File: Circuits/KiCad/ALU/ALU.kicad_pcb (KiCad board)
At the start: 2 copper layers, 131.4 x 86.4 mm, 30 parts, among them J1 Conn_01x13_Male, J2 Conn_01x13_Male, U1 74x377, U10 74x08, U11 74x27, U12 74x245, U2 74x377, U3 74x04, U4 74x181, U5 74x181, U6 74x245, U7 74x08, U8 74x32, U9 74x27

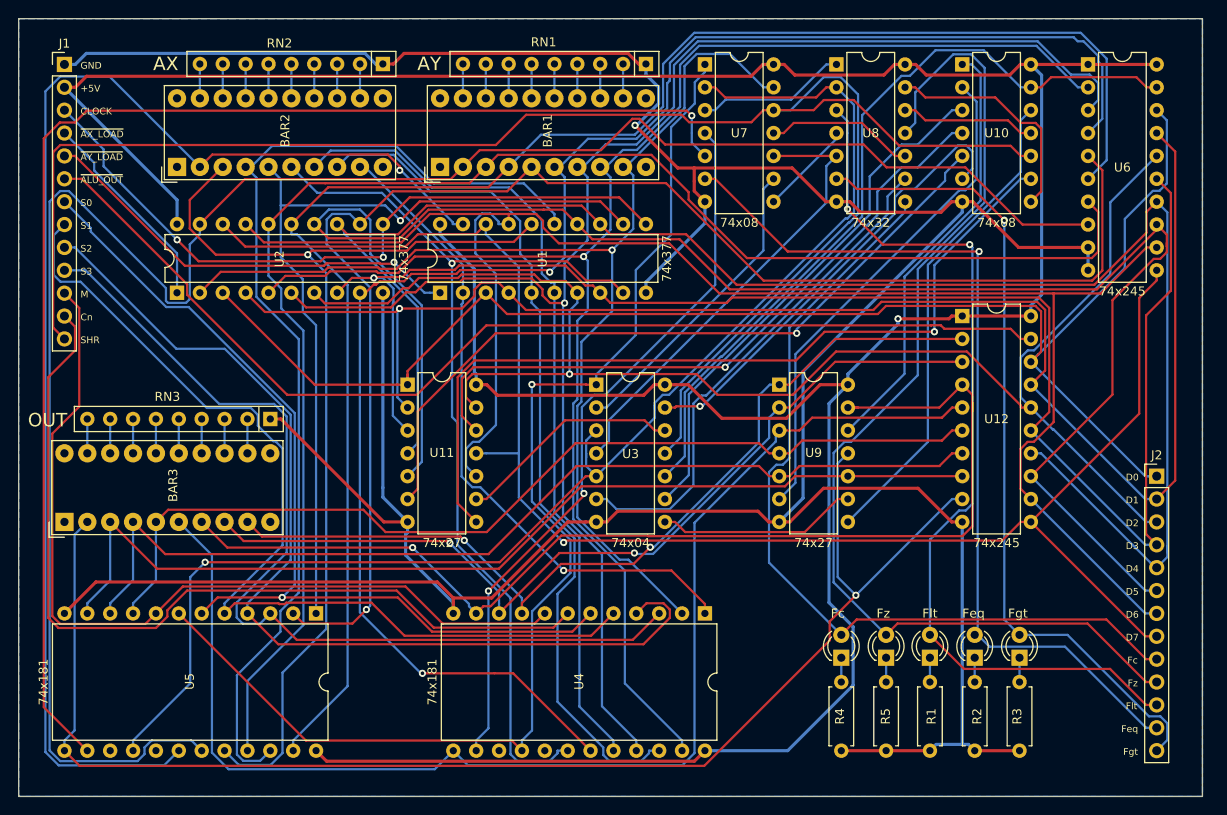
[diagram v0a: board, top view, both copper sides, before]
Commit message: Updated pin header row pitch
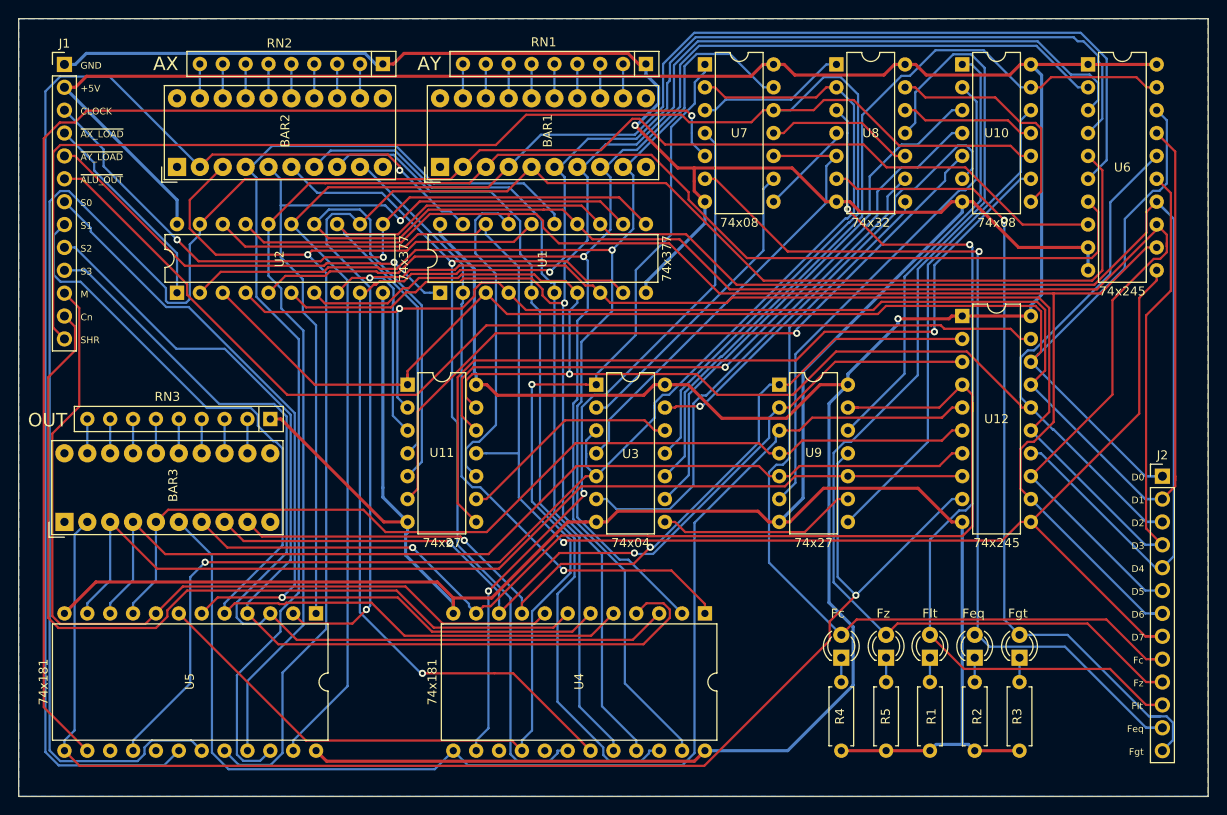
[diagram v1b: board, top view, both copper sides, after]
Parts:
- moved J2 0.64 mm to (144.1, 69.8)
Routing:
- net DATA_BUS2: track 167.7 -> 170.8 mm
- net DATA_BUS1: track 175.5 -> 177.7 mm
- net DATA_BUS3: track 178.5 -> 180.4 mm
- net DATA_BUS7: track 180.7 -> 182.6 mm
- net Feq: track 100.9 -> 102.7 mm
- net Fgt: track 91.3 -> 93.0 mm
- net DATA_BUS4: track 193.1 -> 194.7 mm
- net Fz: track 121.1 -> 122.3 mm
- net Flt: track 100.9 -> 102.2 mm
- net Fc: track 95.7 -> 96.9 mm
- net DATA_BUS6: track 191.4 -> 192.5 mm
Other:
- board size 131.4 x 86.4 mm -> 132.1 x 86.4 mm
